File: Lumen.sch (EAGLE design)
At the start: 1 part, among them U1 Tiny45-20-SMT

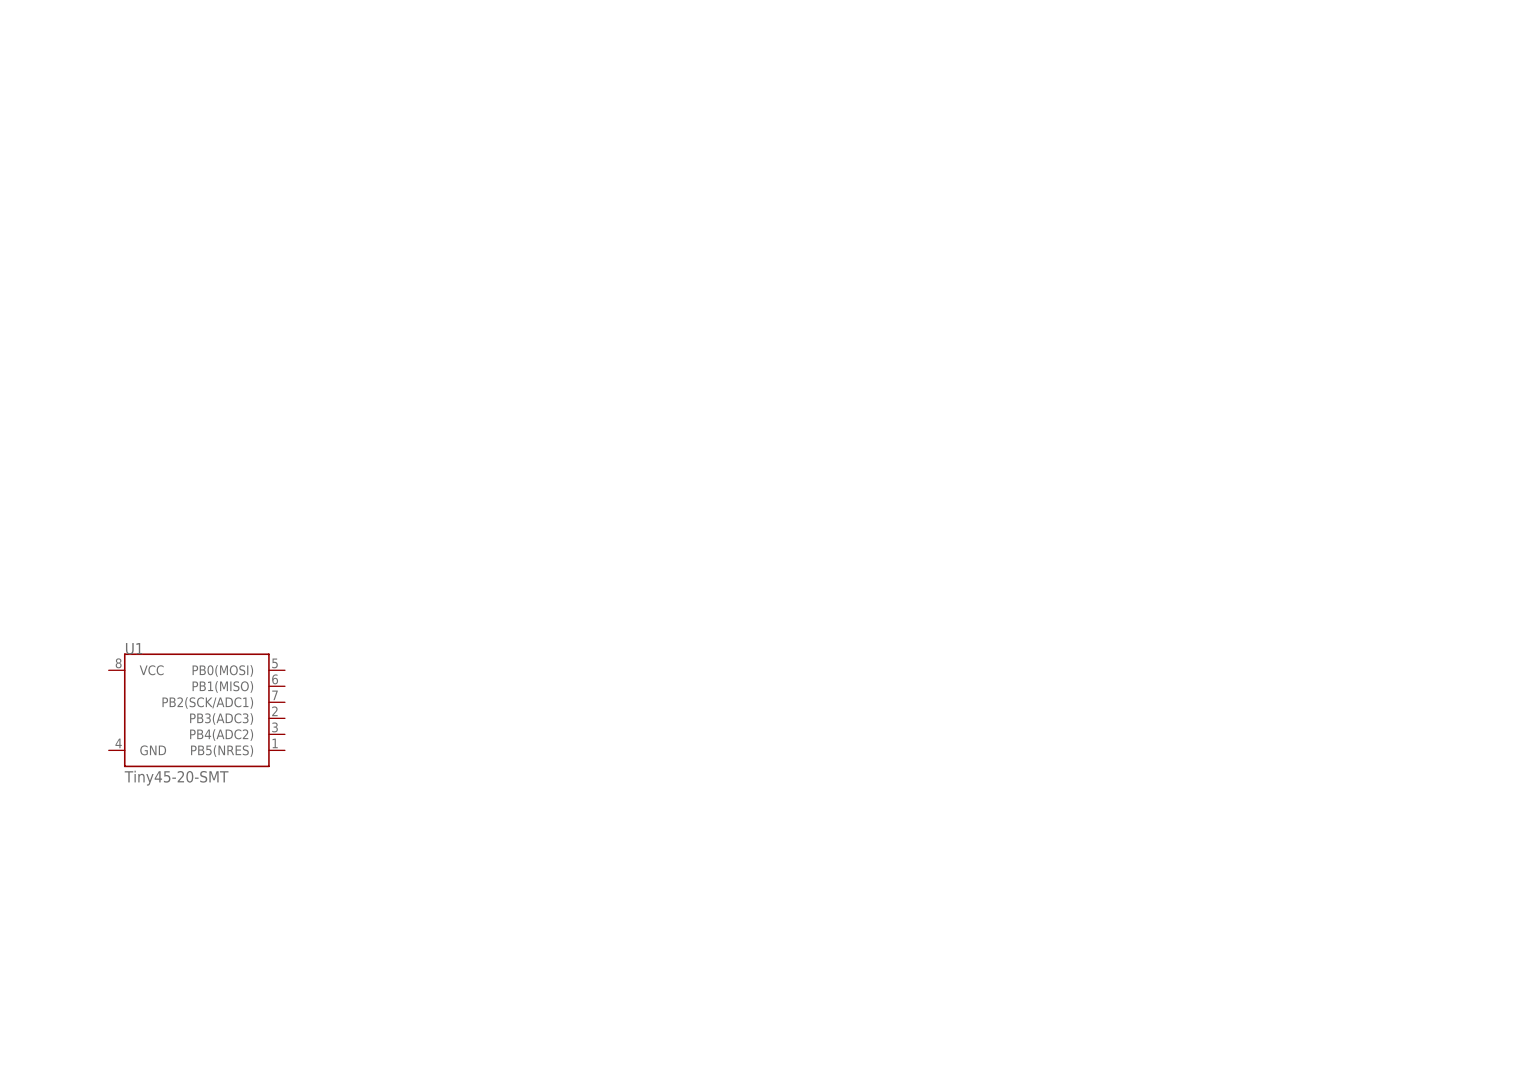
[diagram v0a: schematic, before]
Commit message: Added main components to schematic and wired.
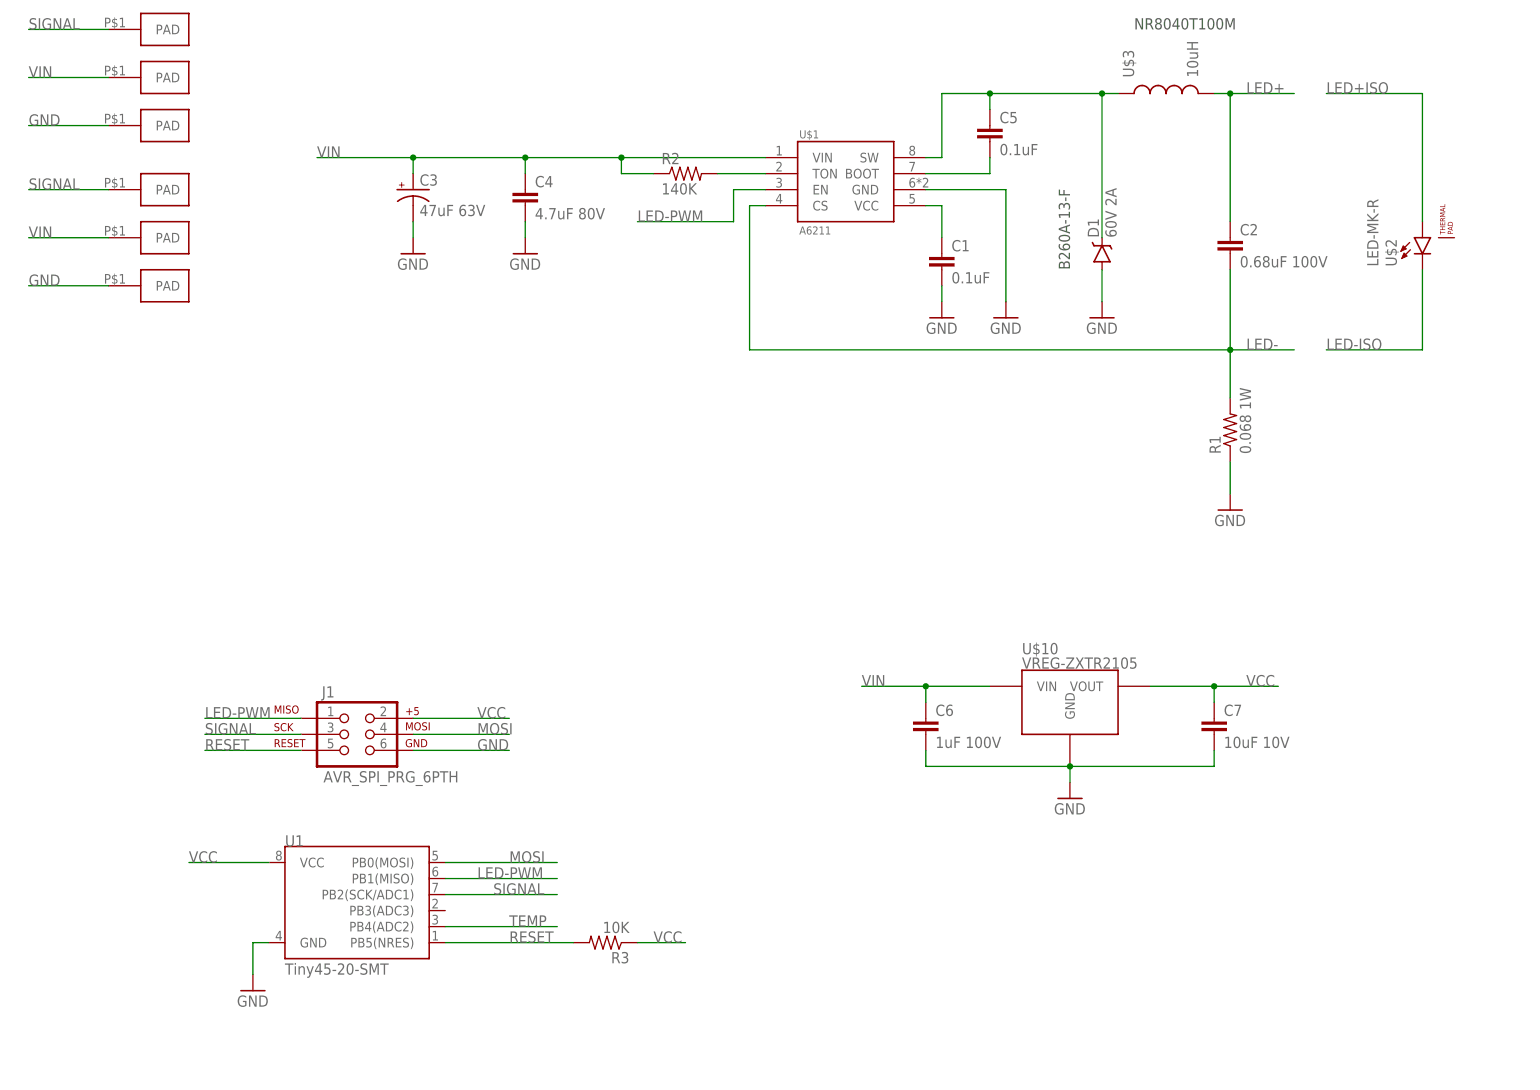
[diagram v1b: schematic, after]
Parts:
- added C1, C5: 0.1uF, resistor:C-EUC0603
- added C2: 0.68uF 100V, resistor:C-EUC1206
- added C3: 47uF 63V, SparkFun-Capacitors:CAP_POLH13
- added C4: 4.7uF 80V, resistor:C-EUC1210
- added C6: 1uF 100V, resistor:C-EUC1206
- added C7: 10uF 10V, resistor:C-EUC0805
- added D1: 60V 2A, SparkFun-DiscreteSemi:DIODE-SCHOTTKY-B340A
- added J1: AVR_SPI_PRG_6PTH, SparkFun-Connectors:AVR_SPI_PRG_6PTH
- added R1: 0.068 1W, resistor:R-US_R1210
- added R2: 140K, resistor:R-US_R0603
- added R3: 10K, resistor:R-US_R0603
- added U$1: A6211, BlueRobotics-Main:A6211
- added U$10: VREG-ZXTR2105, BlueRobotics-Main:VREG-ZXTR2105
- added U$2: LED-MK-R, BlueRobotics-Main:LED-MK-R
- added U$3: 10uH, BlueRobotics-Main:INDUCTOR8040
- added U$4, U$5, U$6, U$7, U$8, U$9: PAD1.5X3MM, BlueRobotics-Main:PAD1.5X3MM
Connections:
- new net GND: C1.2, C3.-, C4.2, C6.2, C7.2, D1.A, J1.6, R1.1, U$1.GND, U$10.GND, U$6.PAD, U$9.PAD, U1.GND
- new net LED+: C2.1, U$3.2
- new net LED+ISO: U$2.A
- new net LED-: C2.2, R1.2, U$1.CS
- new net LED-ISO: U$2.C
- new net LED-PWM: J1.1, U$1.EN, U1.PB1(MISO)
- new net MOSI: J1.4, U1.PB0(MOSI)
- new net N$1: R2.2, U$1.TON
- new net N$4: C5.2, U$1.BOOT
- new net N$5: C5.1, D1.C, U$1.SW, U$3.1
- new net N$8: C1.1, U$1.VCC
- new net RESET: J1.5, R3.2, U1.PB5(NRES)
- new net SIGNAL: J1.3, U$4.PAD, U$7.PAD, U1.PB2(SCK/ADC1)
- new net TEMP: U1.PB4(ADC2)
- new net VCC: C7.1, J1.2, R3.1, U$10.VOUT, U1.VCC
- new net VIN: C3.+, C4.1, C6.1, R2.1, U$1.VIN, U$10.VIN, U$5.PAD, U$8.PAD
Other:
- note added: "B260A-13-F"
- note added: "NR8040T100M"
- moved on the sheet: U1

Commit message: Added thermistor.
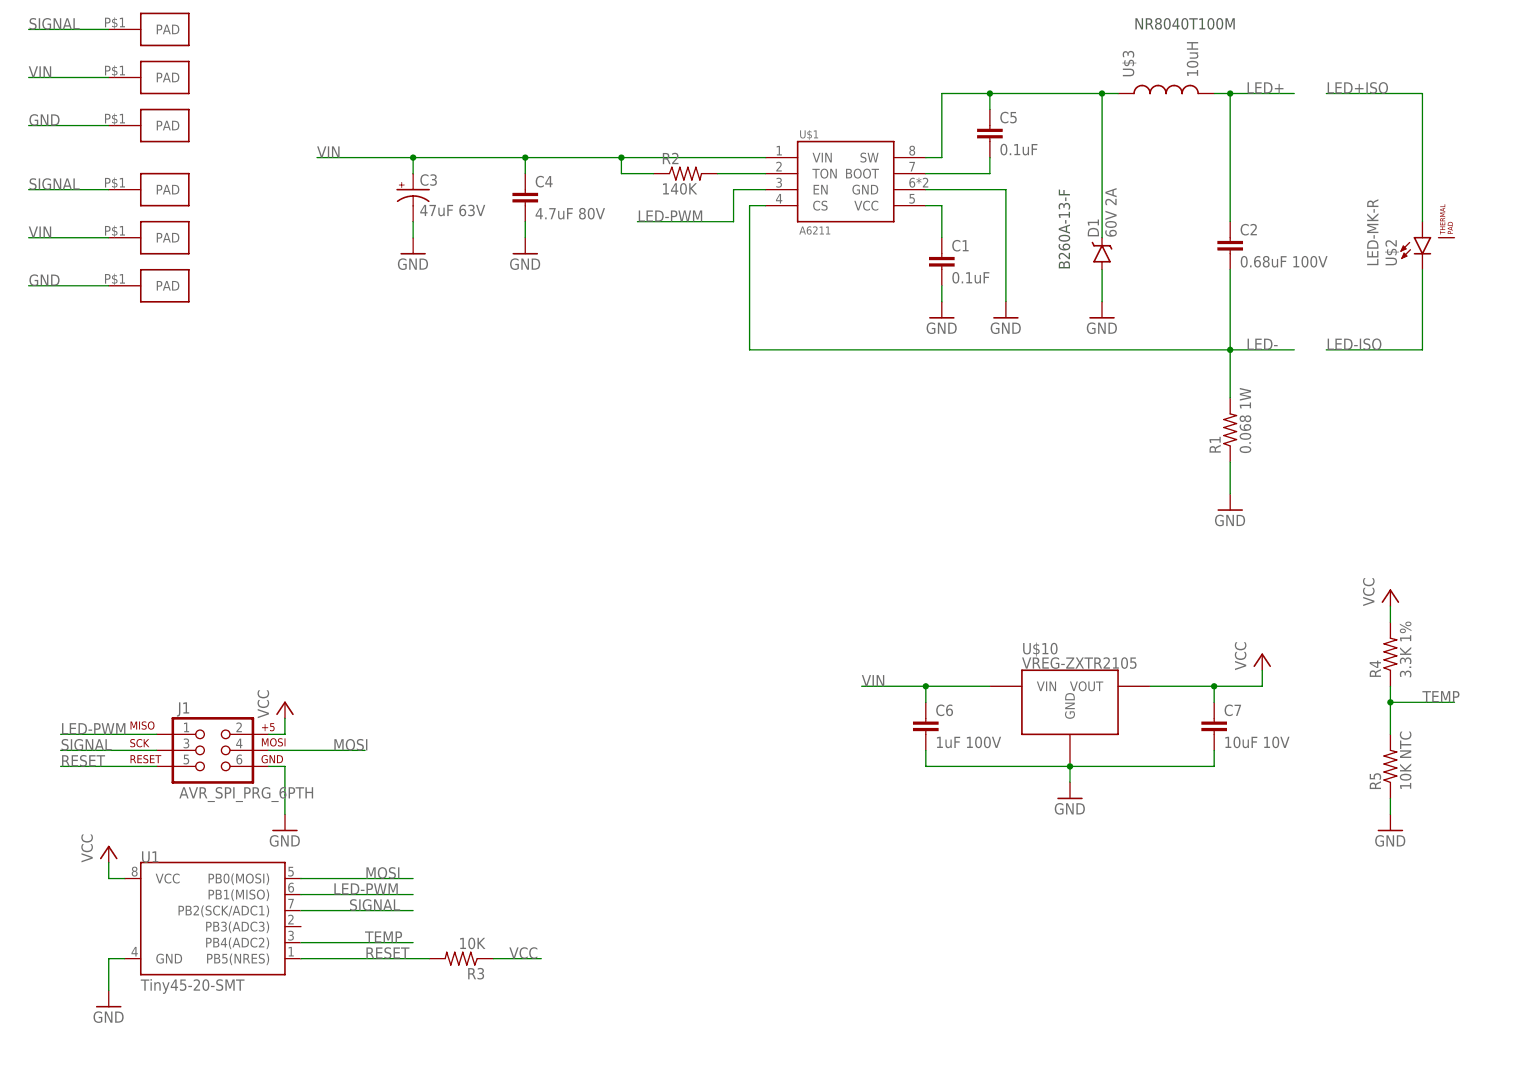
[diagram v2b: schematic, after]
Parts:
- added R4: 3.3K 1%, resistor:R-US_R0603
- added R5: 10K NTC, resistor:R-US_R0603
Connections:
- net GND: now also R5.1
- net TEMP: now also R4.1, R5.2
- net VCC: now also R4.2
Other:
- moved on the sheet: J1, R3, U1

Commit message: Added completed board layout and made some changes to the schematic. Nearly ready for prototype.
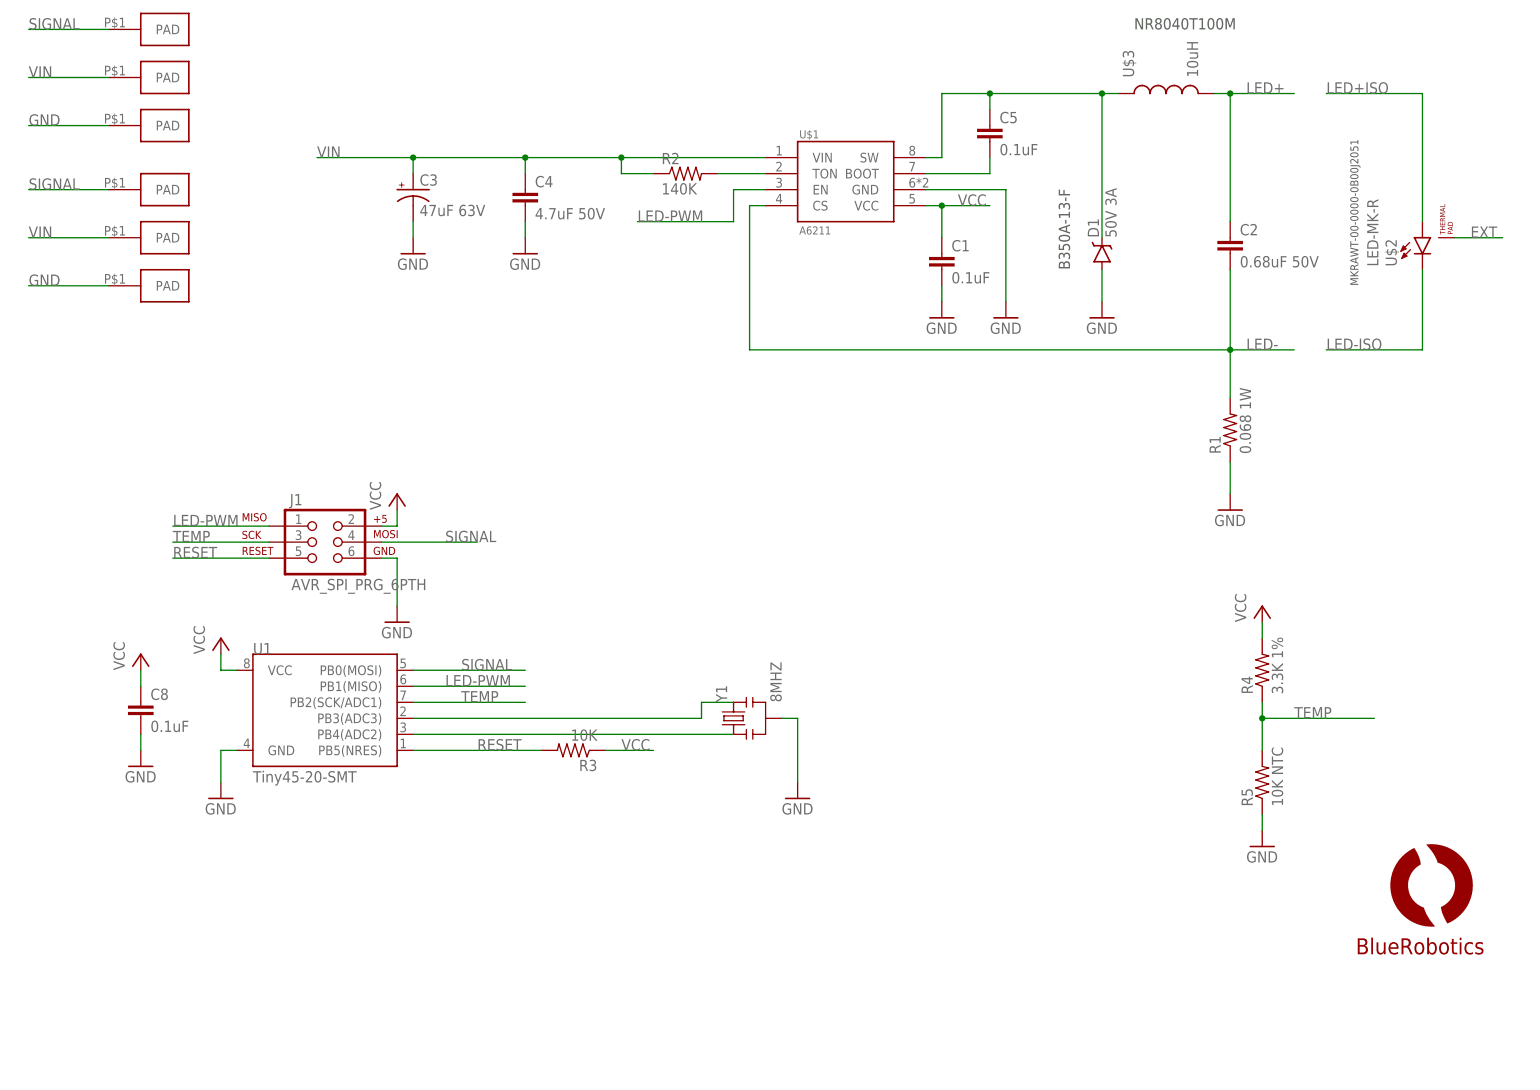
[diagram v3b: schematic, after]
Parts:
- removed C6: 1uF 100V, resistor:C-EUC1206
- removed C7: 10uF 10V, resistor:C-EUC0805
- added C8: 0.1uF, resistor:C-EUC0603
- added Y1: 8MHZ, SparkFun-FreqCtrl:RESONATOR16MHZ
- C2: value 0.68uF 100V -> 0.68uF 50V; device resistor:C-EUC1206 -> resistor:C-EUC0805
- C3: device SparkFun-Capacitors:CAP_POLH13 -> SparkFun-Capacitors:CAP_POLPTH1
- C4: value 4.7uF 80V -> 4.7uF 50V; device resistor:C-EUC1210 -> resistor:C-EUC1206
- D1: value 60V 2A -> 50V 3A
- U$10: value VREG-ZXTR2105 -> LOGOBR-LOGO-MS; device BlueRobotics-Main:VREG-ZXTR2105 -> BlueRobotics-Main:LOGOBR-LOGO-MS
- U$4, U$5, U$6, U$7, U$8, U$9: value PAD1.5X3MM -> PAD2X3MM; device BlueRobotics-Main:PAD1.5X3MM -> BlueRobotics-Main:PAD2X3MM
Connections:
- removed net MOSI: J1.4, U1.PB0(MOSI)
- removed net N$8: C1.1, U$1.VCC
- new net EXT: U$2.THERMAL
- new net N$6: U1.PB4(ADC2), Y1.1
- new net N$7: U1.PB3(ADC3), Y1.3
- net GND: now also C8.2, Y1.2; no longer C6.2, C7.2, U$10.GND
- net SIGNAL: now also J1.4, U1.PB0(MOSI); no longer J1.3, U1.PB2(SCK/ADC1)
- net TEMP: now also J1.3, U1.PB2(SCK/ADC1); no longer U1.PB4(ADC2)
- net VCC: now also C1.1, C8.1, U$1.VCC; no longer C7.1, U$10.VOUT
- net VIN: no longer C6.1, U$10.VIN
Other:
- note added: "B350A-13-F"
- note added: "MKRAWT-00-0000-0B00J2051"
- note removed: "B260A-13-F"
- moved on the sheet: J1, R3, R4, R5, U1
